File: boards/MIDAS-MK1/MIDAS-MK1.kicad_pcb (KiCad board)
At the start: 4 copper layers, 60 x 100 mm, 198 parts, among them J101 USB_C_Receptacle_USB2.0, J102 TERMINAL L, J103 TERMINAL R, J104 PJS008-4100-0-VE, J105 CS, J106 POWER, J107 RESET, J401 732511153, J402 732511153, Q1 DMNH6022SSDQ, Q201 DMNH6022SSDQ, Q202 DMNH6022SSDQ, Q204 DMNH6022SSDQ, Q205 DMNH6022SSDQ, SW101 SW_PUSH_RESET, SW102 SW_Push, U101 TCAL9539-Q1, U102 TCAL9539-Q1, U103 TCAL9539-Q1, U104 ESP32-S3-WROOM-1U, U105 ECMF02-2AMX6, U106 ADS7138-Q1, U107 MCP251863, U108 MTFCxxxx, U201 LM74670-Q1, U301 TPS2121, U302 TI_TPS566242DRLR, U303 TI_TPS566242DRLR, U401 RFM96W-433S2, U402 BGA725L6, U403 Teseo-LIV3R, U501 ADXL355, U502 BNO086, U503 LIS3MDL, U504 LSM6DSLTR, U505 KX134-1211, U506 MS5611-01BA03, Y101 Crystal 40MHz, Y501 32.768kHz

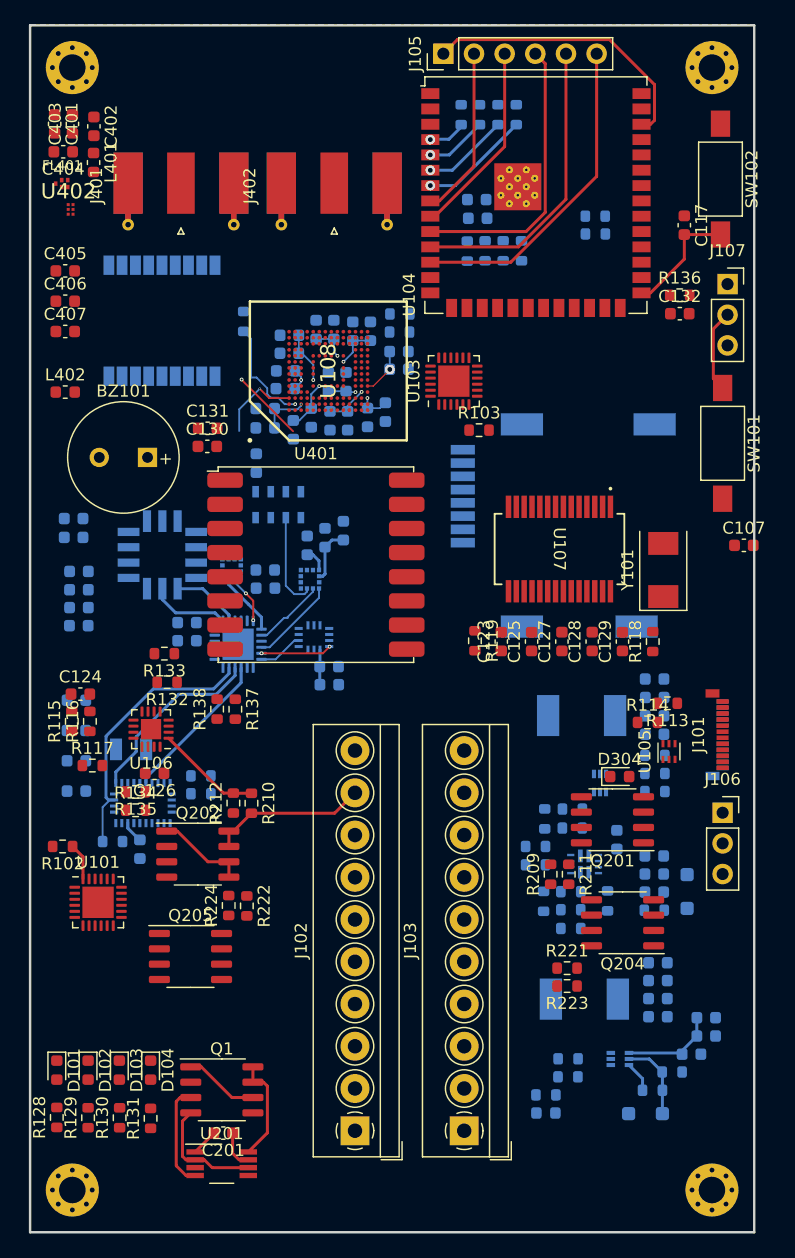
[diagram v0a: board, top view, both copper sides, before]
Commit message: added CAN connector
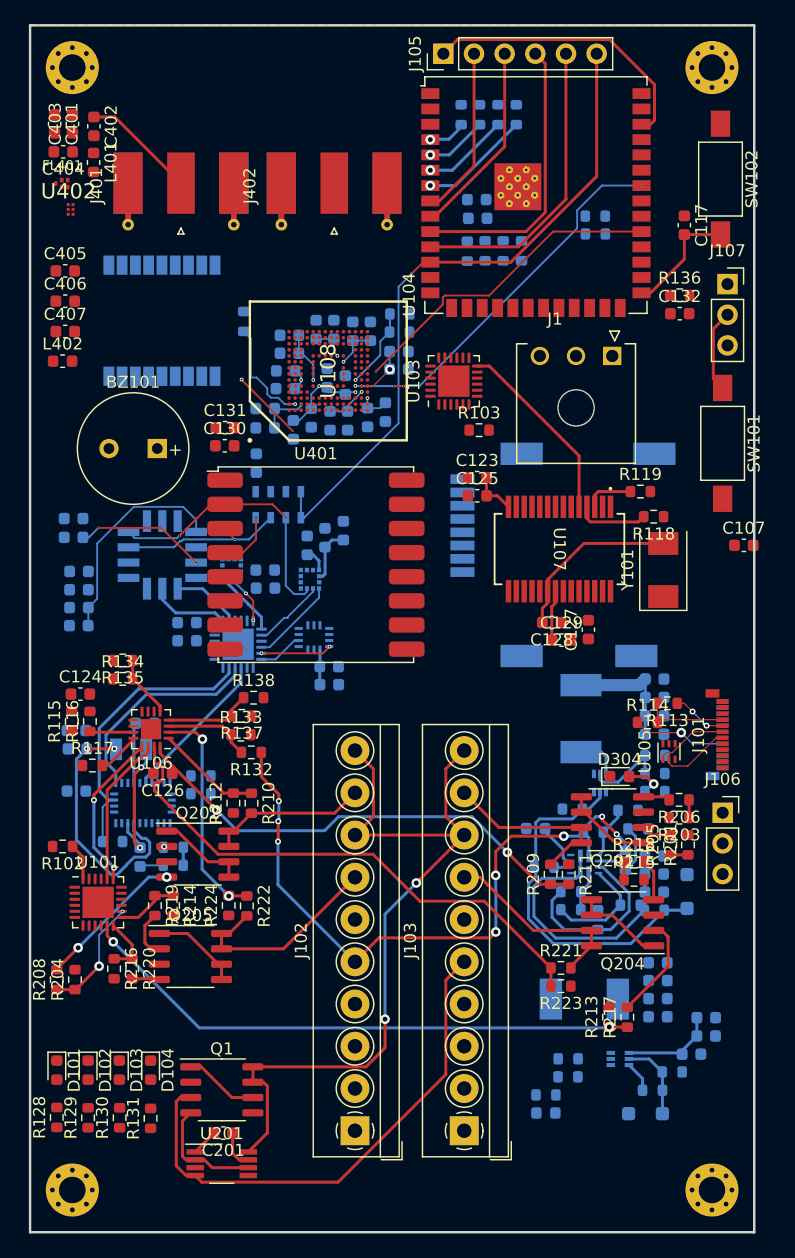
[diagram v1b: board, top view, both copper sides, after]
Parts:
- added J1: 2157601003, Connector_Molex_CAN:MOLEX_2157601003, F.Cu at (153.2, 77.4)
- added R201: 3.3k, Resistor_SMD:R_0603_1608Metric, F.Cu at (159.5, 117.9)
- added R202: 3.3k, Resistor_SMD:R_0603_1608Metric, B.Cu at (116.9, 119.6)
- added R203: 3.3k, Resistor_SMD:R_0603_1608Metric, F.Cu at (158.8, 115.6)
- added R204: 3.3k, Resistor_SMD:R_0603_1608Metric, F.Cu at (108.7, 129.1)
- added R205: 1k, Resistor_SMD:R_0603_1608Metric, F.Cu at (158.0, 117.9)
- added R206: 1k, Resistor_SMD:R_0603_1608Metric, F.Cu at (158.8, 114.2)
- added R207: 1k, Resistor_SMD:R_0603_1608Metric, B.Cu at (116.9, 118.1)
- added R208: 1k, Resistor_SMD:R_0603_1608Metric, F.Cu at (107.2, 129.1)
- added R213: 3.3k, Resistor_SMD:R_0603_1608Metric, F.Cu at (153.0, 132.2)
- added R214: 3.3k, Resistor_SMD:R_0603_1608Metric, F.Cu at (116.8, 122.9)
- added R215: 3.3k, Resistor_SMD:R_0603_1608Metric, F.Cu at (155.0, 120.8)
- added R216: 3.3k, Resistor_SMD:R_0603_1608Metric, F.Cu at (112.0, 128.2)
- added R217: 1k, Resistor_SMD:R_0603_1608Metric, F.Cu at (154.5, 132.2)
- added R218: 1k, Resistor_SMD:R_0603_1608Metric, F.Cu at (155.0, 119.3)
- added R219: 1k, Resistor_SMD:R_0603_1608Metric, F.Cu at (115.3, 122.9)
- added R220: 1k, Resistor_SMD:R_0603_1608Metric, F.Cu at (113.5, 128.2)
- moved R119 18.5 mm to (155.6, 88.6), turned to 0 degrees
- moved C123 13.7 mm to (142.0, 87.5), turned to 0 degrees
- moved C125 12.9 mm to (142.1, 89.0), turned to 0 degrees
- moved R134 10.9 mm to (112.7, 104.2)
- moved R135 10.9 mm to (112.7, 102.6)
- moved R118 10.3 mm to (156.7, 90.7), turned to 180 degrees
- moved R133 9.23 mm to (122.5, 108.8), turned to 0 degrees
- moved R132 9.08 mm to (123.3, 110.2)
- moved R308 8.99 mm to (155.4, 116.6), turned to 0 degrees
- moved R307 7.53 mm to (154.3, 119.2), turned to -90 degrees
- moved R306 6.93 mm to (154.5, 115.0), turned to 0 degrees
- moved C301 6.79 mm to (146.9, 116.5), turned to 0 degrees
- moved C513 5.99 mm to (114.5, 107.8)
- moved R309 5.95 mm to (147.6, 119.8), turned to 0 degrees
- moved R302 5.30 mm to (154.7, 122.9)
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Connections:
- U103 pad 12: unconnected-(U103-P12-Pad12) -> /CAN_STBY
- U403 pad 9: /LIV3F_REST -> /LIV3F_RESET
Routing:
- net /V_pyro: track 8.72 -> 66.2 mm, vias 0 -> 2
- net /VBAT: track 0.00 -> 55.9 mm, vias 0 -> 8
- net /arm_b: track 0.00 -> 47.1 mm, vias 0 -> 2
- net /sense_b: track 0.00 -> 45.1 mm
- net /sense_a: track 0.00 -> 39.9 mm, vias 0 -> 2
- net /VBAT_Pyro: track 8.56 -> 43.2 mm
- net /MEM_CMD: track 0.00 -> 31.4 mm, vias 0 -> 4
- net /Power/5V_EN_VBAT: track 0.00 -> 30.1 mm
- net /MS5611_CS: track 26.9 -> 55.2 mm, vias 0 -> 1
- net /MEM_RST_N: track 0.00 -> 27.2 mm, vias 0 -> 1
- net /Power/Sys_Pow: track 7.98 -> 31.6 mm
- net Net-(U502-XOUT32/CLKSEL1): track 0.00 -> 21.4 mm, vias 0 -> 2
- net /sense_d: track 0.00 -> 18.5 mm, vias 0 -> 2
- net Net-(U501-V1P8DIG): track 0.00 -> 18.0 mm
- net /pyro_d: track 0.00 -> 17.5 mm
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
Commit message: almost there
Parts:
- R103: moved to B.Cu
- moved C401 9.28 mm to (106.6, 67.4)
- moved C403 9.28 mm to (108.1, 67.4)
- moved C405 7.92 mm to (115.1, 73.7), turned to 180 degrees
- moved C407 7.89 mm to (115.1, 72.1), turned to 180 degrees
- moved BZ101 6.54 mm to (109.1, 84.0), turned to 0 degrees
- moved R103 5.71 mm to (137.0, 81.1), turned to 180 degrees
- moved C406 3.47 mm to (107.7, 76.3), turned to 180 degrees
- moved R127 3.25 mm to (153.2, 64.3), turned to 0 degrees
- moved U401 1.69 mm to (130.1, 95.6), turned to 90 degrees
- moved R124 1.40 mm to (153.2, 65.8), turned to 0 degrees
- moved C101 1.03 mm to (129.4, 78.2)
- moved U402 0.74 mm to (107.5, 64.9), turned to -90 degrees
- moved C113 0.38 mm to (130.9, 79.5)
- moved R204 0.29 mm to (109.0, 129.0)
- moved R208 0.29 mm to (107.5, 129.0)
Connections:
- U101 pad 1: /LED_ORANGE -> /EXP_INT1
- U101 pad 16: /LED_RED -> /EXP_INT2
- U101 pad 2: /LED_GREEN -> /LED_RED
- U101 pad 3: /LED_BLUE -> /LED_ORANGE
- U101 pad 4: /EXP_INT1 -> /LED_GREEN
- U101 pad 5: /EXP_INT2 -> /LED_BLUE
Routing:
- net /fire_a: track 1.47 -> 75.9 mm, vias 0 -> 2
- net /SNS_SPI_SCK: track 4.85 -> 77.9 mm, vias 1 -> 9
- net /EXP_INT2: track 0.00 -> 66.2 mm, vias 0 -> 4
- net /Buzzer: track 0.00 -> 64.6 mm, vias 0 -> 1
- net /BNO086_INT: track 0.00 -> 62.4 mm, vias 0 -> 3
- net /arm_a: track 1.48 -> 63.5 mm, vias 0 -> 2
- net /fire_b: track 1.51 -> 52.9 mm, vias 0 -> 2
- net /MicroSD_DAT0: track 0.00 -> 47.5 mm, vias 0 -> 3
- net /ADXL355_CS: track 14.1 -> 61.0 mm, vias 0 -> 3
- net /MicroSD_CMD: track 0.00 -> 44.3 mm, vias 0 -> 1
- net /SNS_SPI_MISO: track 22.9 -> 65.1 mm, vias 2 -> 7
- net /MicroSD_CLK: track 0.00 -> 39.8 mm, vias 0 -> 1
- net /RFM96W_CS: track 0.00 -> 38.8 mm, vias 0 -> 2
- net Net-(J402-In): track 0.00 -> 38.7 mm, vias 0 -> 2
- net /LIV3F_RESET: track 0.00 -> 38.1 mm, vias 0 -> 1
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
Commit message: Continuing routing
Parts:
- moved C509 1.33 mm to (117.3, 100.6), turned to 90 degrees
- moved C511 0.87 mm to (118.8, 100.6), turned to -90 degrees
- moved C124 0.53 mm to (109.7, 105.4)
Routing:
- net /EXP_INT: track 3.18 -> 83.8 mm, vias 1 -> 3
- net /BNO086_CS: track 16.2 -> 87.4 mm, vias 0 -> 7
- net /USB_D-: track 0.00 -> 65.4 mm, vias 0 -> 8
- net /USB_D+: track 0.00 -> 57.8 mm, vias 0 -> 8
- net /RESET_SW: track 6.87 -> 49.5 mm, vias 0 -> 2
- net /KX134_CS: track 23.7 -> 62.3 mm, vias 0 -> 5
- net /USB_Power: track 10.5 -> 46.9 mm, vias 0 -> 1
- net /EXP_INT1: track 0.00 -> 32.9 mm, vias 0 -> 1
- net /I2C_SDA: track 38.7 -> 67.6 mm, vias 3 -> 4
- net /SNS_SPI_SCK: track 77.9 -> 106.8 mm, vias 9 -> 12
- net /EXP_RESET: track 8.17 -> 36.5 mm, vias 1 -> 2
- net /SNS_SPI_MOSI: track 22.1 -> 48.3 mm, vias 3 -> 7
- net /I2C_SCL: track 37.9 -> 60.7 mm, vias 4 -> 5
- net /CAN_NINT0: track 0.00 -> 17.3 mm, vias 0 -> 4
- net Net-(U107-RXCAN): track 0.00 -> 10.5 mm, vias 0 -> 2
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
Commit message: Continuing routing
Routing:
- net /LSM6DSL_CS: track 23.7 -> 83.5 mm, vias 0 -> 3
- net /SNS_SPI_MOSI: track 48.3 -> 49.5 mm
- net /RFM96W_INT: track 31.3 -> 30.7 mm

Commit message: Continuing routing
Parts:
- moved U402 0.15 mm to (107.4, 65.0), turned to 0 degrees
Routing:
- net /I2C_SCL: track 60.7 -> 92.6 mm, vias 5 -> 7
- net /I2C_SDA: track 67.6 -> 98.5 mm, vias 4 -> 5
- net Net-(FL401-IN): track 1.75 -> 2.62 mm
- net Net-(U402-AI): track 5.39 -> 4.53 mm
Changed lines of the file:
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@@
   )
   (footprint "RF_Amplifier_Infineon:TSNP-6-2" (layer "F.Cu")
-    (at 107.51 64.945 -90)
+    (at 107.365 64.95)
     (descr "TSNP-6-2 Infineon 0.7x1.1mm")
     (tags "TSNP-6-2 Infineon 0.7x1.1mm")
@@
     (property "ki_keywords" "Low Noise Amplifier GNSS 20db 3.6mA Infineon")
     (attr smd)
-    (fp_text reference "U402" (at 0 -1.5 90) (layer "F.SilkS")
+    (fp_text reference "U402" (at 0 -1.5) (layer "F.SilkS")
         (effects (font (size 1.27 1.27) (thickness 0.254)))
     )
-    (fp_text value "BGA725L6" (at 0 1.5 90) (layer "F.SilkS") hide
+    (fp_text value "BGA725L6" (at 0 1.5) (layer "F.SilkS") hide
         (effects (font (size 1.27 1.27) (thickness 0.254)))
     )
@@
       )
       (stroke (width 0.1) (type solid)) (fill none) (layer "F.Fab"))
-    (pad "1" smd rect (at -0.025 -0.4) (size 0.25 0.25) (layers "F.Cu" "F.Paste" "F.Mask")
+    (pad "1" smd rect (at -0.025 -0.4 90) (size 0.25 0.25) (layers "F.Cu" "F.Paste" "F.Mask")
       (net 2 "GND") (pinfunction "GND") (pintype "power_in"))
-    (pad "2" smd rect (at -0.025 0) (size 0.25 0.25) (layers "F.Cu" "F.Paste" "F.Mask")
+    (pad "2" smd rect (at -0.025 0 90) (size 0.25 0.25) (layers "F.Cu" "F.Paste" "F.Mask")
       (net 6 "+3V3") (pinfunction "VCC") (pintype "power_in"))
-    (pad "3" smd rect (at -0.025 0.4) (size 0.25 0.25) (layers "F.Cu" "F.Paste" "F.Mask")
+    (pad "3" smd rect (at -0.025 0.4 90) (size 0.25 0.25) (layers "F.Cu" "F.Paste" "F.Mask")
       (net 34 "Net-(FL401-IN)") (pinfunction "AO") (pintype "output"))
-    (pad "4" smd rect (at 0.375 0.4) (size 0.25 0.25) (layers "F.Cu" "F.Paste" "F.Mask")
+    (pad "4" smd rect (at 0.375 0.4 90) (size 0.25 0.25) (layers "F.Cu" "F.Paste" "F.Mask")
       (net 2 "GND") (pinfunction "GNDRF") (pintype "power_in"))
-    (pad "5" smd rect (at 0.375 0) (size 0.25 0.25) (layers "F.Cu" "F.Paste" "F.Mask")
+    (pad "5" smd rect (at 0.375 0 90) (size 0.25 0.25) (layers "F.Cu" "F.Paste" "F.Mask")
       (net 68 "Net-(U402-AI)") (pinfunction "AI") (pintype "input"))
-    (pad "6" smd rect (at 0.375 -0.4) (size 0.25 0.25) (layers "F.Cu" "F.Paste" "F.Mask")
+    (pad "6" smd rect (at 0.375 -0.4 90) (size 0.25 0.25) (layers "F.Cu" "F.Paste" "F.Mask")
       (net 313 "unconnected-(U402-PON-Pad6)") (pinfunction "PON") (pintype "input+no_connect"))
     (model "${ISS_3DMODEL_DIR}/RF_Amplifier_Infineon.3dshapes/TSNP-6-2.stp"
@@
   (segment (start 156.674596 112.860858) (end 156.567542 112.860858) (width 0.25) (layer "B.Cu") (net 33))
   (segment (start 156.567542 112.860858) (end 155.9438 113.4846) (width 0.25) (layer "B.Cu") (net 33))
-  (segment (start 107.1198 63.1109) (end 107.1198 64.85878) (width 0.16) (layer "F.Cu") (net 34))
+  (segment (start 106.935 63.2957) (end 106.935 65.19098) (width 0.16) (layer "F.Cu") (net 34))
+  (segment (start 107.1198 63.1109) (end 106.935 63.2957) (width 0.16) (layer "F.Cu") (net 34))
+  (segment (start 106.935 65.19098) (end 107.09902 65.355) (width 0.16) (layer "F.Cu") (net 34))
+  (segment (start 107.09902 65.355) (end 107.335 65.355) (width 0.16) (layer "F.Cu") (net 34))
   (segment (start 161.0505 108.0262) (end 162.3822 108.0262) (width 0.1) (layer "F.Cu") (net 35))
   (segment (start 161.05 108.0257) (end 161.0505 108.0262) (width 0.1) (layer "F.Cu") (net 35))
@@
   (segment (start 152.3474 110.217) (end 152.7222 110.5918) (width 0.25) (layer "B.Cu") (net 67))
   (segment (start 150.6474 110.217) (end 152.3474 110.217) (width 0.25) (layer "B.Cu") (net 67))
-  (segment (start 108.14891 65.72) (end 110.2614 63.60751) (width 0.15) (layer "F.Cu") (net 68))
-  (segment (start 107.67109 65.72) (end 108.14891 65.72) (width 0.15) (layer "F.Cu") (net 68))
-  (segment (start 107.51 65.32) (end 107.51 65.55891) (width 0.15) (layer "F.Cu") (net 68))
+  (segment (start 108.91891 64.95) (end 110.2614 63.60751) (width 0.15) (layer "F.Cu") (net 68))
+  (segment (start 107.74 64.95) (end 108.91891 64.95) (width 0.15) (layer "F.Cu") (net 68))
   (segment (start 110.2614 63.60751) (end 110.2614 62.1539) (width 0.15) (layer "F.Cu") (net 68))
-  (segment (start 107.51 65.55891) (end 107.67109 65.72) (width 0.15) (layer "F.Cu") (net 68))
   (segment (start 155.8264 117.729) (end 153.493152 117.729) (width 0.25) (layer "F.Cu") (net 69))
   (segment (start 150.6764 113.919) (end 150.6764 115.189) (width 0.25) (layer "F.Cu") (net 69))
@@
   (segment (start 138.42048 98.29048) (end 138.42048 83.02048) (width 0.25) (layer "B.Cu") (net 86))
   (segment (start 110.55395 113.49395) (end 114.273 109.7749) (width 0.25) (layer "F.Cu") (net 87))
+  (segment (start 134.38 57.95) (end 122.71 57.95) (width 0.16) (layer "F.Cu") (net 87))
+  (segment (start 119.2256 61.4344) (end 119.2256 69.8728) (width 0.16) (layer "F.Cu") (net 87))
+  (segment (start 136.38 59.95) (end 134.38 57.95) (width 0.16) (layer "F.Cu") (net 87))
   (segment (start 110.346728 113.49395) (end 110.55395 113.49395) (width 0.16) (layer "F.Cu") (net 87))
   (segment (start 107.53 106.85) (end 107.53 110.677222) (width 0.16) (layer "F.Cu") (net 87))
@@
   (segment (start 110.29225 114.196991) (end 110.29225 113.75565) (width 0.25) (layer "F.Cu") (net 87))
   (segment (start 107.525 106.845) (end 107.53 106.85) (width 0.16) (layer "F.Cu") (net 87))
+  (segment (start 122.71 57.95) (end 119.2256 61.4344) (width 0.16) (layer "F.Cu") (net 87))
   (segment (start 111.8853 119.869) (end 111.8853 120.7245) (width 0.25) (layer "F.Cu") (net 87))
   (segment (start 138.176 77.852312) (end 138.176 78.232) (width 0.16) (layer "F.Cu") (net 87))
   (segment (start 138.001844 77.678156) (end 138.176 77.852312) (width 0.16) (layer "F.Cu") (net 87))
+  (via (at 119.2256 69.8728) (size 0.32) (drill 0.16) (layers "F.Cu" "B.Cu") (net 87))
   (via (at 107.525 106.845) (size 0.32) (drill 0.16) (layers "F.Cu" "B.Cu") (net 87))
   (via (at 138.162 63.276) (size 0.8) (drill 0.4) (layers "F.Cu" "B.Cu") (net 87))
+  (via (at 136.38 59.95) (size 0.32) (drill 0.16) (layers "F.Cu" "B.Cu") (net 87))
   (via (at 110.29225 114.196991) (size 0.5) (drill 0.25) (layers "F.Cu" "B.Cu") (net 87))
   (via (at 111.9598 119.7945) (size 0.5) (drill 0.25) (layers "F.Cu" "B.Cu") (net 87))
@@
   (segment (start 111.9598 119.7945) (end 111.9598 119.793462) (width 0.25) (layer "B.Cu") (net 87))
   (segment (start 138.63 63.744) (end 138.162 63.276) (width 0.16) (layer "B.Cu") (net 87))
+  (segment (start 138.162 63.276) (end 136.38 61.494) (width 0.16) (layer "B.Cu") (net 87))
   (segment (start 137.951844 75.702356) (end 137.951844 72.928156) (width 0.16) (layer "B.Cu") (net 87))
   (segment (start 137.951844 72.928156) (end 138.63 72.25) (width 0.16) (layer "B.Cu") (net 87))
+  (segment (start 136.38 61.494) (end 136.38 59.95) (width 0.16) (layer "B.Cu") (net 87))
   (segment (start 138.001844 77.678156) (end 138.001844 75.752356) (width 0.16) (layer "B.Cu") (net 87))
   (segment (start 111.8398 102.5302) (end 120.2977 102.5302) (width 0.16) (layer "B.Cu") (net 87))
@@
   (segment (start 110.9553 116.08) (end 111.3853 116.51) (width 0.16) (layer "F.Cu") (net 88))
   (segment (start 137.412 62.006) (end 138.162 62.006) (width 0.16) (layer "F.Cu") (net 88))
+  (segment (start 137.65818 62.006) (end 138.162 62.006) (width 0.16) (layer "F.Cu") (net 88))
   (segment (start 136.99 68.4) (end 136.32 67.73) (width 0.16) (layer "F.Cu") (net 88))
   (segment (start 137.4585 78.452) (end 137.4585 76.0615) (width 0.16) (layer "F.Cu") (net 88))
   (segment (start 137.591844 75.922184) (end 137.591844 75.918156) (width 0.16) (layer "F.Cu") (net 88))
+  (segment (start 132.25 58.39) (end 134.04218 58.39) (width 0.16) (layer "F.Cu") (net 88))
   (segment (start 137.591844 75.918156) (end 137.61 75.9) (width 0.16) (layer "F.Cu") (net 88))
   (segment (start 137.591844 75.928156) (end 137.591844 75.922184) (width 0.16) (layer "F.Cu") (net 88))
@@
   (segment (start 108.33 116.08) (end 110.9553 116.08) (width 0.16) (layer "F.Cu") (net 88))
   (segment (start 114.496008 110.5174) (end 114.2326 110.5174) (width 0.25) (layer "F.Cu") (net 88))
+  (segment (start 134.04218 58.39) (end 137.65818 62.006) (width 0.16) (layer "F.Cu") (net 88))
   (segment (start 111.3853 116.51) (end 111.3853 120.7245) (width 0.25) (layer "F.Cu") (net 88))
   (segment (start 137.4585 76.0615) (end 137.591844 75.928156) (width 0.16) (layer "F.Cu") (net 88))
+  (via (at 132.25 58.39) (size 0.32) (drill 0.16) (layers "F.Cu" "B.Cu") (net 88))
   (via (at 137.591844 75.922184) (size 0.2) (drill 0.16) (layers "F.Cu" "B.Cu") (net 88))
   (via (at 136.99 68.4) (size 0.2) (drill 0.16) (layers "F.Cu" "B.Cu") (net 88))
@@
   (segment (start 137.831094 68.999362) (end 137.591844 69.238612) (width 0.16) (layer "B.Cu") (net 88))
   (segment (start 137.573348 68.377108) (end 137.831094 68.634854) (width 0.16) (layer "B.Cu") (net 88))
+  (segment (start 118.1256 69.8728) (end 118.1256 62.0944) (width 0.16) (layer "B.Cu") (net 88))
   (segment (start 107.085 114.835) (end 108.33 116.08) (width 0.16) (layer "B.Cu") (net 88))
   (segment (start 107.085 106.662746) (end 107.085 114.835) (width 0.16) (layer "B.Cu") (net 88))
   (segment (start 139.987 62.006) (end 138.162 62.006) (width 0.25) (layer "B.Cu") (net 88))
+  (segment (start 118.1256 62.0944) (end 121.83 58.39) (width 0.16) (layer "B.Cu") (net 88))
   (segment (start 111.632746 102.115) (end 107.085 106.662746) (width 0.16) (layer "B.Cu") (net 88))
   (segment (start 143.764 58.229) (end 139.987 62.006) (width 0.25) (layer "B.Cu") (net 88))
@@
   (segment (start 137.831094 68.634854) (end 137.831094 68.999362) (width 0.16) (layer "B.Cu") (net 88))
   (segment (start 120.2977 102.0302) (end 120.2129 102.115) (width 0.16) (layer "B.Cu") (net 88))
+  (segment (start 121.83 58.39) (end 132.25 58.39) (width 0.16) (layer "B.Cu") (net 88))
   (segment (start 110.0284 108.5674) (end 109.9566 108.4956) (width 0.25) (layer "F.Cu") (net 89))
   (segment (start 113.5655 108.5674) (end 110.0284 108.5674) (width 0.25) (layer "F.Cu") (net 89))

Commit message: Continuing to route
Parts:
- moved R132 17.6 mm to (126.4, 127.6)
- moved R313 1.50 mm to (149.2, 113.6)
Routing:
- net /VBAT_SENSE: track 7.28 -> 27.5 mm, vias 0 -> 2
- net /VBAT: track 55.6 -> 40.3 mm, vias 6 -> 2
- net /VBAT_Pyro: track 43.2 -> 49.9 mm
- net /sense_b: track 44.8 -> 50.4 mm, vias 0 -> 4
- net /Power/5V_EN_VBAT: track 30.1 -> 35.6 mm, vias 0 -> 2
- net /sense_a: track 40.1 -> 44.0 mm
- net Net-(Q204B-G2): track 3.49 -> 7.37 mm
- net /V_pyro: track 66.6 -> 70.1 mm, vias 2 -> 0
- net /SNS_SPI_SCK: track 106.9 -> 103.5 mm
- net /pyro_c: track 13.0 -> 16.2 mm, vias 1 -> 0
- net /EXP_INT2: track 66.2 -> 63.3 mm
- net /USB_Power: track 46.9 -> 49.5 mm
- net Net-(Q201A-G1): track 2.47 -> 4.89 mm
- net /pyro_d: track 17.5 -> 15.1 mm
- net Net-(Q204A-S1): track 7.47 -> 8.62 mm
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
